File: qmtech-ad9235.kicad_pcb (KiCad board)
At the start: 4 copper layers, 55 x 75 mm, 55 parts

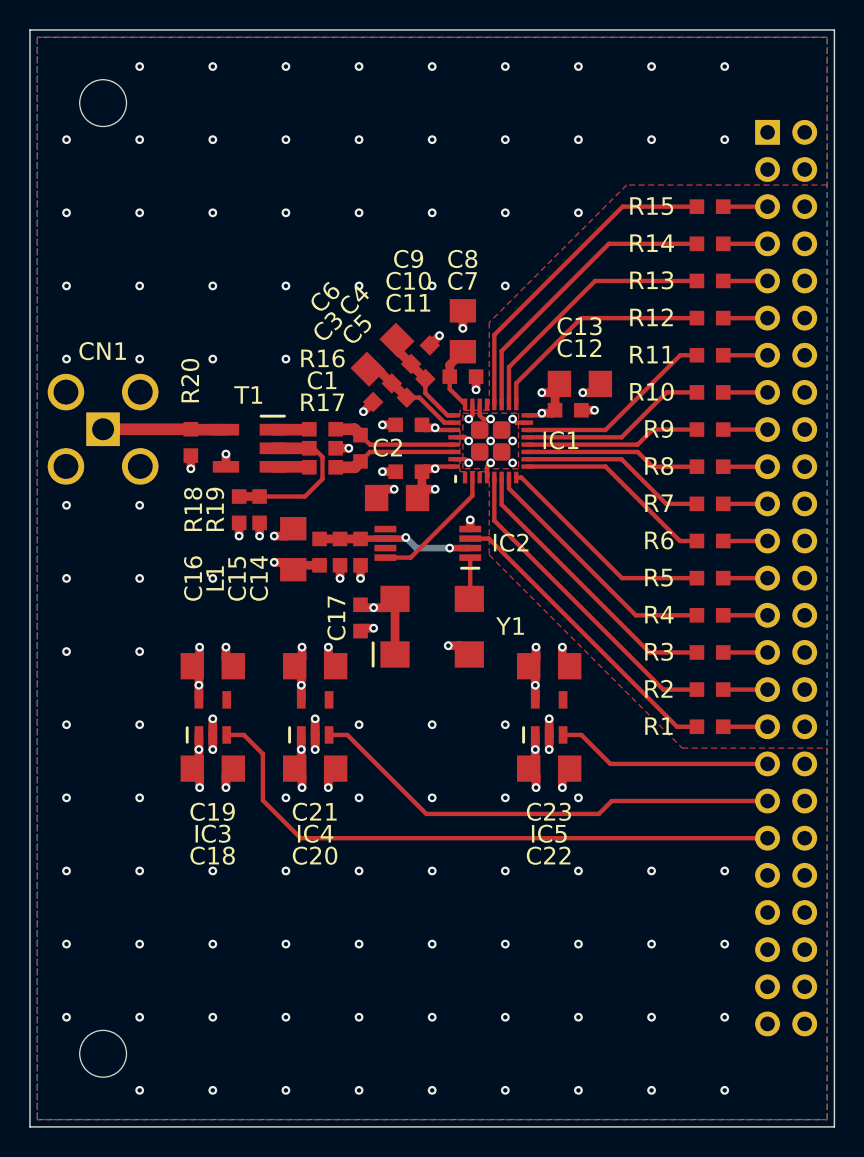
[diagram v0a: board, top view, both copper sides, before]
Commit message: move VCM closer to transformer in qmtech-ad9235
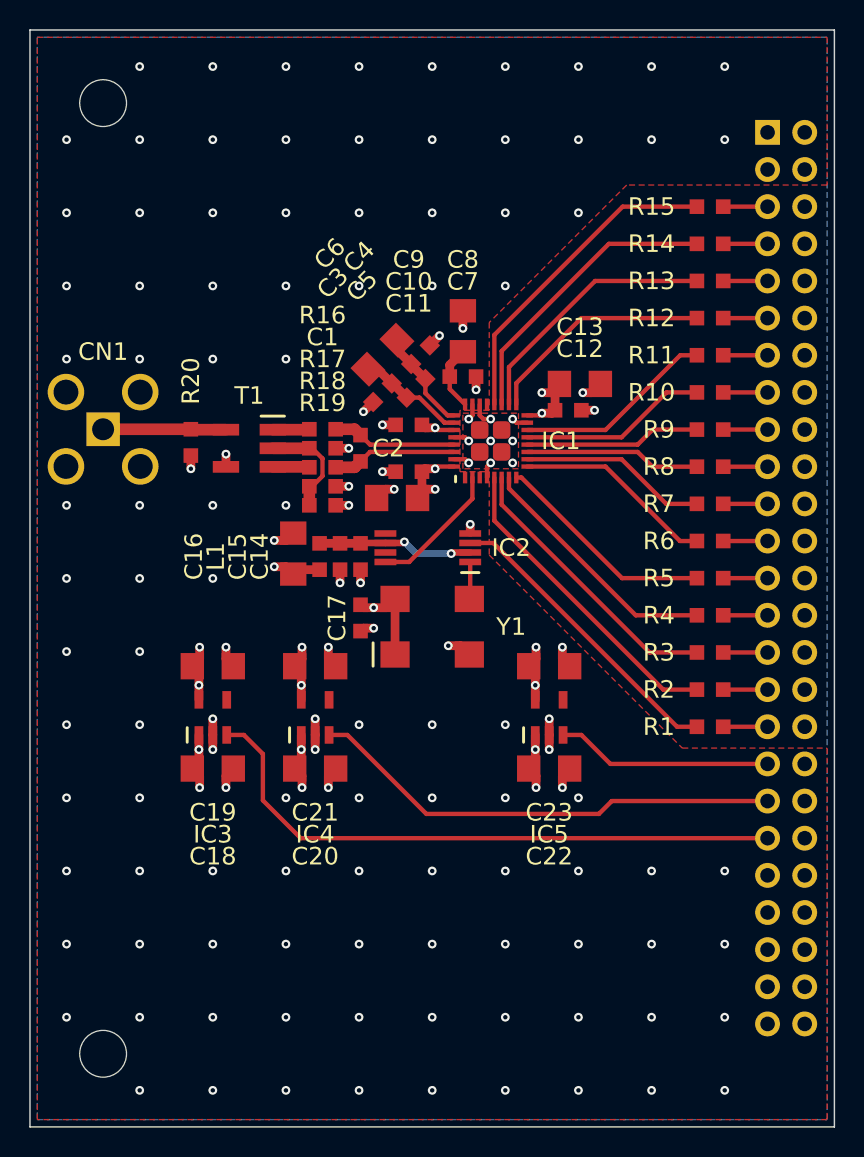
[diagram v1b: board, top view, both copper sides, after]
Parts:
- moved R18 5.92 mm to (140.0, 86.2), turned to 180 degrees
- moved R19 4.31 mm to (140.0, 87.5), turned to 0 degrees
- moved IC2 0.30 mm to (147.2, 90.4)
- moved C14 0.30 mm to (142.6, 91.0)
- moved C15 0.30 mm to (141.2, 91.0)
- moved C16 0.30 mm to (138.0, 90.8)
- moved L1 0.30 mm to (139.8, 91.0)
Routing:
- net VCM: track 11.3 -> 7.38 mm
- net GND: vias 136 -> 138

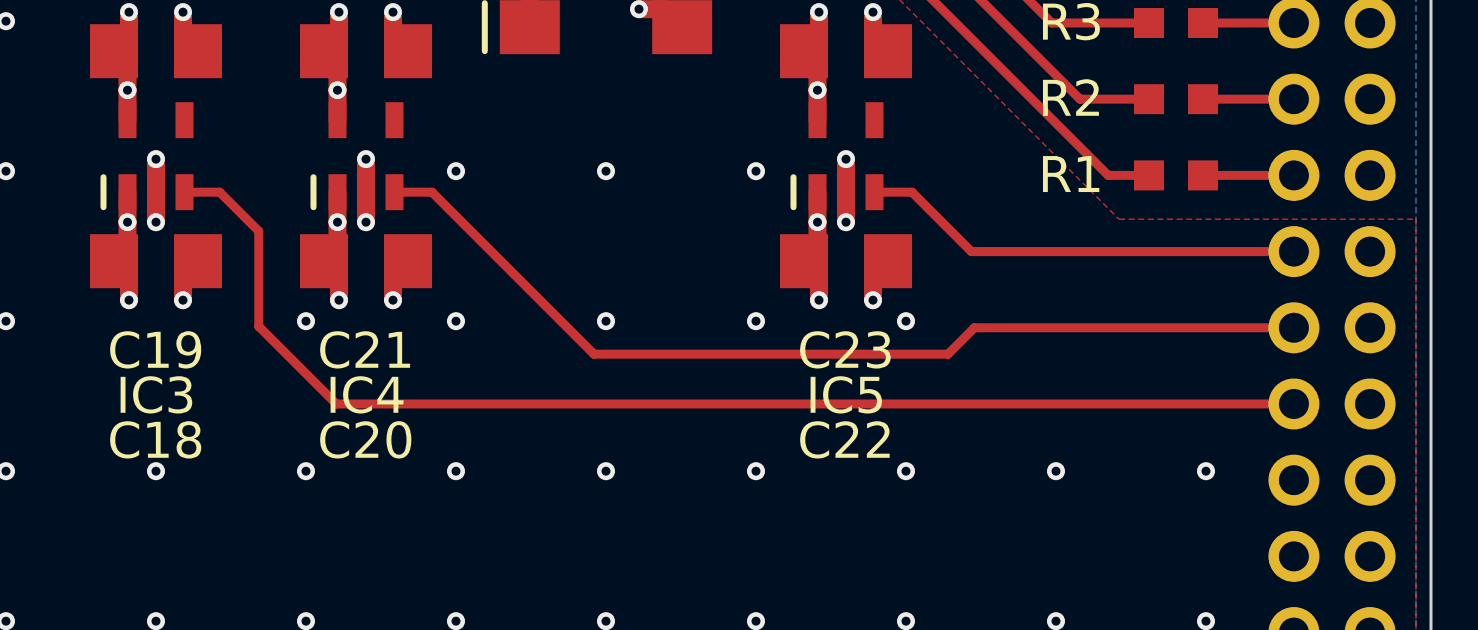
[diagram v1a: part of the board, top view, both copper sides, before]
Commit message: add resistors to FPGA outputs in qmtech-ad9235
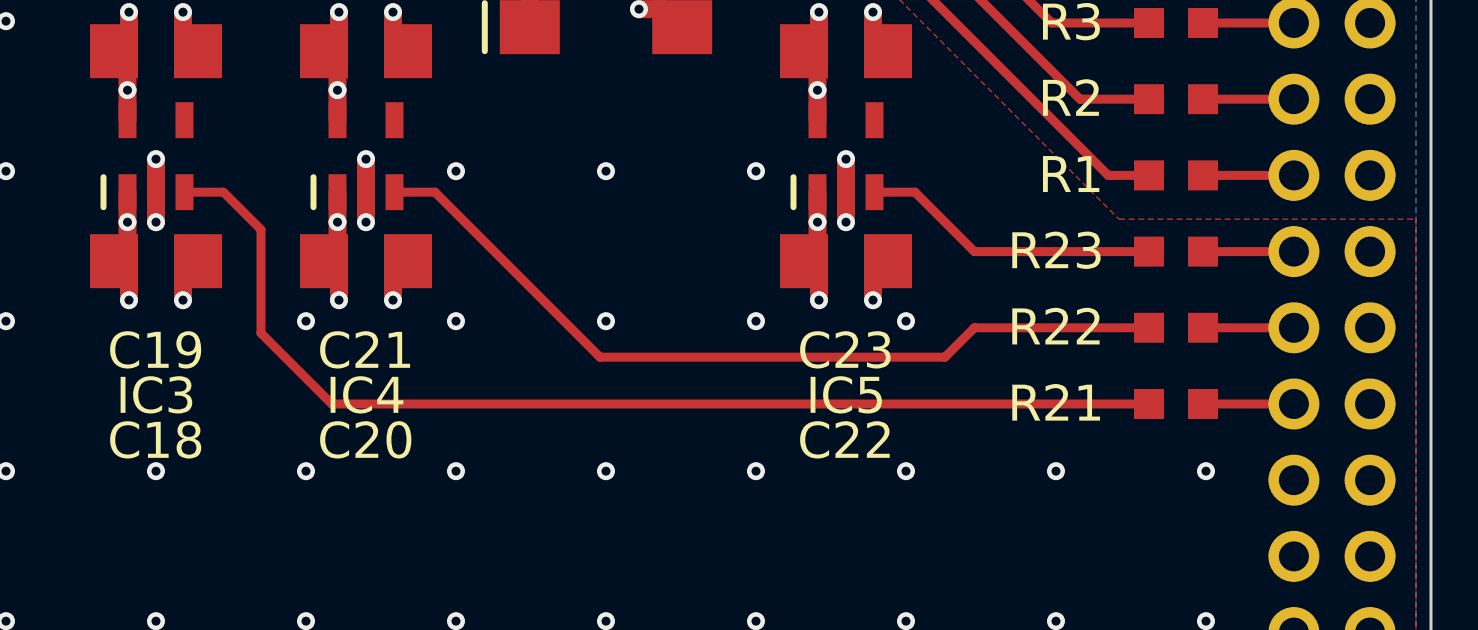
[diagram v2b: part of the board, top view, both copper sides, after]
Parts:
- added R21: , footprints:0603, F.Cu at (166.5, 110.3)
- added R22: , footprints:0603, F.Cu at (166.5, 107.7)
- added R23: , footprints:0603, F.Cu at (166.5, 105.2)
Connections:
- CN2 pad 35: DEN -> W18
- CN2 pad 37: CEN -> W17
- CN2 pad 39: AEN -> W16
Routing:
- net DEN: track 14.8 -> 9.97 mm
- net CEN: track 32.6 -> 27.8 mm
- net AEN: track 41.8 -> 37.1 mm
- net W18: track 0.00 -> 3.03 mm
- net W17: track 0.00 -> 3.03 mm
- net W16: track 0.00 -> 3.03 mm
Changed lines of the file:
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@@
   (net 49 "CVDD")
   (net 50 "CEN")
+  (net 51 "W18")
+  (net 52 "W17")
+  (net 53 "W16")
   (footprint "footprints:0603" (layer "F.Cu")
     (at 145.9 82 180)
@@
     (pad "2" smd rect (at 0.9 0 180) (size 1 1) (layers "F.Cu" "F.Paste" "F.Mask")
       (net 38 "VCM"))
+  )
+  (footprint "footprints:0603" (layer "F.Cu")
+    (at 166.5 105.18)
+    (property "mpn" "C8218")
+    (attr smd)
+    (fp_text reference "R23" (at -4 0) (layer "F.SilkS")
+        (effects (font (size 1.2 1.2) (thickness 0.2)))
+    )
+    (fp_text value "" (at 0 0) (layer "F.SilkS")
+        (effects (font (size 1.27 1.27) (thickness 0.15)))
+    )
+    (fp_text user "${REFERENCE}" (at -4 0) (layer "F.Fab")
+        (effects (font (size 1.2 1.2) (thickness 0.2)))
+    )
+    (pad "1" smd rect (at -0.9 0) (size 1 1) (layers "F.Cu" "F.Paste" "F.Mask")
+      (net 47 "DEN"))
+    (pad "2" smd rect (at 0.9 0) (size 1 1) (layers "F.Cu" "F.Paste" "F.Mask")
+      (net 51 "W18"))
   )
   (footprint "footprints:0603" (layer "F.Cu")
@@
     (pad "2" smd rect (at 0.9 0) (size 1 1) (layers "F.Cu" "F.Paste" "F.Mask")
       (net 27 "W6"))
+  )
+  (footprint "footprints:0603" (layer "F.Cu")
+    (at 166.5 110.26)
+    (property "mpn" "C8218")
+    (attr smd)
+    (fp_text reference "R21" (at -4 0) (layer "F.SilkS")
+        (effects (font (size 1.2 1.2) (thickness 0.2)))
+    )
+    (fp_text value "" (at 0 0) (layer "F.SilkS")
+        (effects (font (size 1.27 1.27) (thickness 0.15)))
+    )
+    (fp_text user "${REFERENCE}" (at -4 0) (layer "F.Fab")
+        (effects (font (size 1.2 1.2) (thickness 0.2)))
+    )
+    (pad "1" smd rect (at -0.9 0) (size 1 1) (layers "F.Cu" "F.Paste" "F.Mask")
+      (net 48 "AEN"))
+    (pad "2" smd rect (at 0.9 0) (size 1 1) (layers "F.Cu" "F.Paste" "F.Mask")
+      (net 53 "W16"))
+  )
+  (footprint "footprints:0603" (layer "F.Cu")
+    (at 166.5 107.72)
+    (property "mpn" "C8218")
+    (attr smd)
+    (fp_text reference "R22" (at -4 0) (layer "F.SilkS")
+        (effects (font (size 1.2 1.2) (thickness 0.2)))
+    )
+    (fp_text value "" (at 0 0) (layer "F.SilkS")
+        (effects (font (size 1.27 1.27) (thickness 0.15)))
+    )
+    (fp_text user "${REFERENCE}" (at -4 0) (layer "F.Fab")
+        (effects (font (size 1.2 1.2) (thickness 0.2)))
+    )
+    (pad "1" smd rect (at -0.9 0) (size 1 1) (layers "F.Cu" "F.Paste" "F.Mask")
+      (net 50 "CEN"))
+    (pad "2" smd rect (at 0.9 0) (size 1 1) (layers "F.Cu" "F.Paste" "F.Mask")
+      (net 52 "W17"))
   )
   (footprint "footprints:SMD7050-4P" (layer "F.Cu")
@@
     (pad "34" thru_hole circle (at -40.64 1.27 90) (size 1.7 1.7) (drill 1) (layers "*.Cu" "*.Mask"))
     (pad "35" thru_hole circle (at -43.18 -1.27 90) (size 1.7 1.7) (drill 1) (layers "*.Cu" "*.Mask")
-      (net 47 "DEN"))
+      (net 51 "W18"))
     (pad "36" thru_hole circle (at -43.18 1.27 90) (size 1.7 1.7) (drill 1) (layers "*.Cu" "*.Mask"))
     (pad "37" thru_hole circle (at -45.72 -1.27 90) (size 1.7 1.7) (drill 1) (layers "*.Cu" "*.Mask")
-      (net 50 "CEN"))
+      (net 52 "W17"))
     (pad "38" thru_hole circle (at -45.72 1.27 90) (size 1.7 1.7) (drill 1) (layers "*.Cu" "*.Mask"))
     (pad "39" thru_hole circle (at -48.26 -1.27 90) (size 1.7 1.7) (drill 1) (layers "*.Cu" "*.Mask")
-      (net 48 "AEN"))
+      (net 53 "W16"))
     (pad "40" thru_hole circle (at -48.26 1.27 90) (size 1.7 1.7) (drill 1) (layers "*.Cu" "*.Mask"))
     (pad "41" thru_hole circle (at -50.8 -1.27 90) (size 1.7 1.7) (drill 1) (layers "*.Cu" "*.Mask"))
@@
   (segment (start 146.4 90.8) (end 145.6 90) (width 0.45) (layer "B.Cu") (net 46))
   (segment (start 148.8 90.8) (end 146.4 90.8) (width 0.45) (layer "B.Cu") (net 46))
-  (segment (start 156.45 103.2) (end 157.7 103.2) (width 0.3) (layer "F.Cu") (net 47))
-  (segment (start 159.68 105.18) (end 170.43 105.18) (width 0.3) (layer "F.Cu") (net 47))
-  (segment (start 157.7 103.2) (end 159.68 105.18) (width 0.3) (layer "F.Cu") (net 47))
-  (segment (start 134.625 103.2) (end 135.925 104.5) (width 0.3) (layer "F.Cu") (net 48))
-  (segment (start 133.45 103.2) (end 134.625 103.2) (width 0.3) (layer "F.Cu") (net 48))
-  (segment (start 135.925 107.675) (end 138.51 110.26) (width 0.3) (layer "F.Cu") (net 48))
-  (segment (start 138.51 110.26) (end 170.43 110.26) (width 0.3) (layer "F.Cu") (net 48))
-  (segment (start 135.925 104.5) (end 135.925 107.675) (width 0.3) (layer "F.Cu") (net 48))
+  (segment (start 165.6 105.18) (end 159.78 105.18) (width 0.3) (layer "F.Cu") (net 47))
+  (segment (start 159.78 105.18) (end 157.8 103.2) (width 0.3) (layer "F.Cu") (net 47))
+  (segment (start 157.8 103.2) (end 156.45 103.2) (width 0.3) (layer "F.Cu") (net 47))
+  (segment (start 138.36 110.26) (end 165.6 110.26) (width 0.3) (layer "F.Cu") (net 48))
+  (segment (start 136 104.45) (end 136 107.9) (width 0.3) (layer "F.Cu") (net 48))
+  (segment (start 133.45 103.2) (end 134.75 103.2) (width 0.3) (layer "F.Cu") (net 48))
+  (segment (start 136 107.9) (end 138.36 110.26) (width 0.3) (layer "F.Cu") (net 48))
+  (segment (start 134.75 103.2) (end 136 104.45) (width 0.3) (layer "F.Cu") (net 48))
   (segment (start 138.55 99.8) (end 138.55 100.8) (width 0.6) (layer "F.Cu") (net 49))
   (segment (start 138.3 91.9) (end 138 92.2) (width 0.6) (layer "F.Cu") (net 49))
@@
   (via (at 136.7 91.7) (size 0.6) (drill 0.3) (layers "F.Cu" "B.Cu") (free) (net 49))
   (via (at 138.55 99.8) (size 0.6) (drill 0.3) (layers "F.Cu" "B.Cu") (free) (net 49))
-  (segment (start 159.78 107.72) (end 170.43 107.72) (width 0.3) (layer "F.Cu") (net 50))
-  (segment (start 158.9 108.6) (end 159.78 107.72) (width 0.3) (layer "F.Cu") (net 50))
-  (segment (start 147.1 108.6) (end 158.9 108.6) (width 0.3) (layer "F.Cu") (net 50))
-  (segment (start 141.7 103.2) (end 147.1 108.6) (width 0.3) (layer "F.Cu") (net 50))
-  (segment (start 140.45 103.2) (end 141.7 103.2) (width 0.3) (layer "F.Cu") (net 50))
+  (segment (start 165.6 107.72) (end 159.78 107.72) (width 0.3) (layer "F.Cu") (net 50))
+  (segment (start 147.3 108.7) (end 141.8 103.2) (width 0.3) (layer "F.Cu") (net 50))
+  (segment (start 159.78 107.72) (end 158.8 108.7) (width 0.3) (layer "F.Cu") (net 50))
+  (segment (start 141.8 103.2) (end 140.45 103.2) (width 0.3) (layer "F.Cu") (net 50))
+  (segment (start 158.8 108.7) (end 147.3 108.7) (width 0.3) (layer "F.Cu") (net 50))
+  (segment (start 170.43 105.18) (end 167.4 105.18) (width 0.3) (layer "F.Cu") (net 51))
+  (segment (start 170.43 107.72) (end 167.4 107.72) (width 0.3) (layer "F.Cu") (net 52))
+  (segment (start 170.43 110.26) (end 167.4 110.26) (width 0.3) (layer "F.Cu") (net 53))
   (zone (net 18) (net_name "GND") (layer "F.Cu") (hatch edge 0.5)
     (connect_pads no (clearance 0.2))
